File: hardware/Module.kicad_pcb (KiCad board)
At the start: 2 copper layers, 47.6 x 109.2 mm, 123 parts, among them J1 Jack, J10 Jack, J11 Jack, J12 Jack, J13 Micro_SD, J14 Jack, J15 Jack, J16 Jack, J17 Power, J18 Jack, J19 Jack, J2 OLED, J4 Jack, J5 Jack, J6 Jack, J7 Jack, J8 Jack, J9 Jack, SW1 Encoder, SW2 Encoder, U1 TL074, U2 TL074, U3 TL074, U4 MCP6004, U5 MCP6002, U6 TLP2361, U7 LM4040C10

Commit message: Release version 0.4.0
Signed-off-by: Petr Horacek <hrck@protonmail.com>
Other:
- board text added: "board v0.4.0"
- board text removed: "board v0.3.0"
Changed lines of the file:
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@@
     (title "Proton")
     (date "2022-03-06")
-    (rev "v0.3.0")
+    (rev "v0.4.0")
     (company "Petr Horáček")
     (comment 1 "petr@zlosynth.com")
@@
     (effects (font (size 1 1) (thickness 0.15)))
   )
-  (gr_text "board v0.3.0" (at 158.77 58.98 90) (layer "F.SilkS")
+  (gr_text "board v0.4.0" (at 158.77 58.98 90) (layer "F.SilkS")
     (effects (font (size 1 1) (thickness 0.15)) (justify left))
   )

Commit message: Release version 0.5.0
Signed-off-by: Petr Horacek <hrck@protonmail.com>
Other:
- board text added: "board v0.5.0"
- board text removed: "board v0.4.0"
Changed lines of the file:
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@@
     (title "Proton")
     (date "2022-03-06")
-    (rev "v0.4.0")
+    (rev "v0.5.0")
     (company "Petr Horáček")
     (comment 1 "petr@zlosynth.com")
@@
     (effects (font (size 1 1) (thickness 0.15)))
   )
-  (gr_text "board v0.4.0" (at 158.77 58.98 90) (layer "F.SilkS")
+  (gr_text "board v0.5.0" (at 158.77 58.98 90) (layer "F.SilkS")
     (effects (font (size 1 1) (thickness 0.15)) (justify left))
   )

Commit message: Place THT on two-layer PCB
Signed-off-by: Petr Horacek <hrck@protonmail.com>
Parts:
- removed C1: 100n, Capacitor_SMD:C_0603_1608Metric_Pad1.08x0.95mm_HandSolder
- removed D1: Schottky, Diode_SMD:D_SOD-123
- removed R21, R26, R27: 100k, Resistor_SMD:R_0603_1608Metric_Pad0.98x0.95mm_HandSolder
- removed R33: 100R, Resistor_SMD:R_0603_1608Metric_Pad0.98x0.95mm_HandSolder
- removed SW2: Encoder, Rotary_Encoder:RotaryEncoder_Alps_EC11E-Switch_Vertical_H20mm
- removed U6: TLP2361, Package_SO:SO-6L_10x3.84mm_P1.27mm
- added J20: Conn_02x08_Odd_Even, Connector_PinHeader_2.54mm:PinHeader_2x08_P2.54mm_Vertical, B.Cu at (144.6, 58.1)
- added J21: Conn_02x08_Odd_Even, Connector_PinSocket_2.54mm:PinSocket_2x08_P2.54mm_Vertical, F.Cu at (62.6, 56.9)
- added J22: Conn_02x08_Odd_Even, Connector_PinHeader_2.54mm:PinHeader_2x08_P2.54mm_Vertical, B.Cu at (119.5, 58.1)
- added J23: Conn_02x08_Odd_Even, Connector_PinHeader_2.54mm:PinHeader_2x08_P2.54mm_Vertical, B.Cu at (119.5, 93.0)
- added J3: Conn_02x08_Odd_Even, Connector_PinSocket_2.54mm:PinSocket_2x08_P2.54mm_Vertical, F.Cu at (37.5, 56.9)
- added REF**: MountingHole_3.2mm_M3, MountingHole:MountingHole_3.2mm_M3, F.Cu at (160.2, 117.5)
- added REF**: MountingHole_3.2mm_M3, MountingHole:MountingHole_3.2mm_M3, B.Cu at (78.2, 116.3)
- added RV1: Pot, Potentiometer_THT:Potentiometer_Alpha_RD901F-40-00D_Single_Vertical, B.Cu at (53.2, 87.2)
- J1, J4: footprint Custom:Jack_3.5mm_QingPu_WQP-PJ398SM_Vertical_CircularHoles_Stereo -> Connector_Audio:Jack_3.5mm_QingPu_WQP-PJ398SM_Vertical_CircularHoles
- J14: value Jack -> Conn_02x08_Odd_Even; footprint Connector_Audio:Jack_3.5mm_QingPu_WQP-PJ398SM_Vertical_CircularHoles -> Connector_PinSocket_2.54mm:PinSocket_2x08_P2.54mm_Vertical; moved to F.Cu
- R1: value 33R -> 33k
- R15, R20: value 100k -> 100R
- R2: value 220R -> 33k
- R3: value 10R -> 100k
- R9: value 33k -> 100k
- moved R20 255.5 mm to (-111.0, 121.3)
- moved R37 255.5 mm to (-125.2, 122.9)
- moved C11 255.5 mm to (-128.8, 130.7)
- moved C2 255.5 mm to (-121.2, 122.9)
- moved C3 255.5 mm to (-114.2, 133.5)
- moved C4 255.5 mm to (-130.5, 133.5)
- moved R1 255.5 mm to (-104.9, 127.7)
- moved R12 255.5 mm to (-121.2, 124.5)
- moved R13 255.5 mm to (-115.8, 133.5)
- moved R18 255.5 mm to (-120.7, 119.9)
- moved R30 255.5 mm to (-123.9, 120.0)
- moved R36 255.5 mm to (-132.2, 133.5)
- moved R5 255.5 mm to (-110.4, 125.4)
- moved U3 255.5 mm to (-123.2, 130.0)
- moved C10 255.5 mm to (-117.6, 130.6)
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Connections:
- net ENC1_A renamed ENC_A
- net ENC1_B renamed ENC_B
- net ENC1_CLICK renamed ENC_CLICK
- A1 pad 13: ENC2_CLICK -> unconnected-(A1-Pad13)
- A1 pad 14: ENC2_B -> unconnected-(A1-Pad14)
- A1 pad 15: ENC2_A -> unconnected-(A1-Pad15)
- A1 pad 32: MIDI_IN -> unconnected-(A1-Pad32)
- A1 pad 33: MIDI_OUT -> unconnected-(A1-Pad33)
- J1 pad T: Net-(D1-Pad2) -> Net-(J1-PadT)
- J11 pad TN: unconnected-(J11-PadTN) -> Net-(J11-PadTN)
- J12 pad TN: unconnected-(J12-PadTN) -> Net-(J12-PadTN)
- J16 pad TN: Net-(J16-PadTN) -> unconnected-(J16-PadTN)
- J19 pad TN: Net-(J19-PadTN) -> unconnected-(J19-PadTN)
- J2 pad 3: OLED_CS -> OLED_SCK
- J2 pad 4: OLED_CMD -> OLED_DATA
- J2 pad 6: OLED_DATA -> OLED_CMD
- J2 pad 7: OLED_SCK -> OLED_CS
- R1 pad 1: +3V3 -> GND
- R1 pad 2: Net-(J4-PadR) -> Net-(R1-Pad2)
- R15 pad 2: Net-(R15-Pad2) -> Net-(J8-PadT)
- R2 pad 1: Net-(J1-PadR) -> GND
- R2 pad 2: Net-(D1-Pad1) -> Net-(R2-Pad2)
- R20 pad 1: Net-(R14-Pad2) -> Net-(R20-Pad1)
- R20 pad 2: Net-(R20-Pad2) -> Net-(J7-PadT)
- R3 pad 1: MIDI_OUT -> Net-(R1-Pad2)
- R3 pad 2: Net-(J4-PadT) -> Net-(R15-Pad1)
- R32 pad 1: Net-(R26-Pad2) -> Net-(R14-Pad2)
- R32 pad 2: Net-(J7-PadT) -> Net-(J1-PadT)
- R4 pad 2: Net-(J5-PadTN) -> Net-(J15-PadTN)
- R40 pad 2: Net-(J11-PadT) -> Net-(J16-PadT)
- R41 pad 2: Net-(J12-PadT) -> Net-(J19-PadT)
- R45 pad 2: Net-(J16-PadTN) -> Net-(J12-PadTN)
- R46 pad 2: Net-(J15-PadTN) -> Net-(J6-PadTN)
- R47 pad 2: Net-(J14-PadTN) -> Net-(J4-PadTN)
- R49 pad 1: Net-(J18-PadT) -> Net-(J11-PadT)
- R5 pad 2: Net-(J6-PadTN) -> Net-(J18-PadTN)
- R51 pad 1: Net-(J19-PadT) -> Net-(J5-PadT)
- R53 pad 1: Net-(J14-PadT) -> Net-(J4-PadT)
- R57 pad 2: Net-(J18-PadTN) -> Net-(J11-PadTN)
- R58 pad 2: Net-(J19-PadTN) -> Net-(J5-PadTN)
- R6 pad 1: Net-(J5-PadT) -> Net-(J15-PadT)
- R60 pad 1: Net-(J15-PadT) -> Net-(J6-PadT)
- R62 pad 1: Net-(J16-PadT) -> Net-(J12-PadT)
- R7 pad 1: Net-(J6-PadT) -> Net-(J18-PadT)
- R8 pad 1: GATE1 -> GND
- R9 pad 1: GATE2 -> Net-(R2-Pad2)
- R9 pad 2: Net-(R15-Pad1) -> Net-(R20-Pad1)
- U1 pad 10: GND -> Net-(R1-Pad2)
- U1 pad 12: GND -> unconnected-(U1-Pad12)
- U1 pad 13: Net-(R21-Pad2) -> unconnected-(U1-Pad13)
- U1 pad 14: Net-(R27-Pad2) -> unconnected-(U1-Pad14)
- U1 pad 3: GND -> GATE1
- U1 pad 5: GND -> Net-(R2-Pad2)
- U1 pad 6: Net-(R20-Pad2) -> GATE2
- U1 pad 7: Net-(R26-Pad2) -> Net-(R20-Pad1)
- U1 pad 8: Net-(R15-Pad2) -> Net-(R15-Pad1)
- U1 pad 9: Net-(R15-Pad1) -> GATE3
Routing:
- net VCC: track 267.2 -> 0.00 mm, vias 7 -> 0
- net +3V3: track 178.6 -> 0.00 mm, vias 3 -> 0
- net VEE: track 156.2 -> 0.00 mm, vias 4 -> 0
- net GND: track 127.6 -> 0.00 mm, vias 37 -> 0
- net -10V: track 104.5 -> 0.00 mm, vias 13 -> 0
- net PROBE: track 102.1 -> 0.00 mm, vias 4 -> 0
- net MIDI_IN: track 94.9 -> 0.00 mm, vias 6 -> 0
- net +3.3VA: track 84.1 -> 0.00 mm, vias 9 -> 0
- net MIDI_OUT: track 81.4 -> 0.00 mm, vias 3 -> 0
- net DAC2: track 69.1 -> 0.00 mm, vias 4 -> 0
- net DAC1: track 64.7 -> 0.00 mm, vias 4 -> 0
- net GATE2: track 63.1 -> 0.00 mm, vias 2 -> 0
- net GATE1: track 59.2 -> 0.00 mm, vias 2 -> 0
- net CV3: track 53.5 -> 0.00 mm
- net CV2: track 49.2 -> 0.00 mm
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- removed copper zone on B.Cu, net GND
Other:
- board size 47.6 x 109.2 mm -> 129.5 x 110.4 mm
- board text added: "Jack"
- board text removed: "S. jack"
- board text removed: "Take care not to damage SMD parts while soldering"

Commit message: Wire up all connections
Signed-off-by: Petr Horacek <hrck@protonmail.com>
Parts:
- removed the REF** at (160.2, 117.5)
- removed the REF** at (78.2, 116.3)
- J14: value Conn_02x08_Odd_Even -> NW_B; footprint Connector_PinSocket_2.54mm:PinSocket_2x08_P2.54mm_Vertical -> Connector_PinSocket_2.54mm:PinSocket_2x06_P2.54mm_Vertical
- J20: value Conn_02x08_Odd_Even -> SW_B; footprint Connector_PinHeader_2.54mm:PinHeader_2x08_P2.54mm_Vertical -> Connector_PinSocket_2.54mm:PinSocket_2x06_P2.54mm_Vertical; moved to F.Cu
- J21: value Conn_02x08_Odd_Even -> NW_A; footprint Connector_PinSocket_2.54mm:PinSocket_2x08_P2.54mm_Vertical -> Connector_PinHeader_2.54mm:PinHeader_2x06_P2.54mm_Vertical; moved to B.Cu
- J22: value Conn_02x08_Odd_Even -> SW_A; footprint Connector_PinHeader_2.54mm:PinHeader_2x08_P2.54mm_Vertical -> Connector_PinHeader_2.54mm:PinHeader_2x06_P2.54mm_Vertical
- J23: value Conn_02x08_Odd_Even -> NE_A; footprint Connector_PinHeader_2.54mm:PinHeader_2x08_P2.54mm_Vertical -> Connector_PinHeader_2.54mm:PinHeader_2x06_P2.54mm_Vertical
- J3: value Conn_02x08_Odd_Even -> NE_B; footprint Connector_PinSocket_2.54mm:PinSocket_2x08_P2.54mm_Vertical -> Connector_PinSocket_2.54mm:PinSocket_2x06_P2.54mm_Vertical
- moved R1 262.5 mm to (152.0, 74.0), turned to 0 degrees
- moved R36 261.7 mm to (129.2, 122.0), turned to 180 degrees
- moved C11 260.3 mm to (131.5, 130.8), turned to -90 degrees
- moved C4 259.9 mm to (129.2, 124.4), turned to 0 degrees
- moved R31 257.2 mm to (130.6, 143.8), turned to 90 degrees
- moved R37 255.0 mm to (129.2, 140.2), turned to 0 degrees
- moved C5 254.8 mm to (129.2, 137.7), turned to 180 degrees
- moved R3 254.0 mm to (152.0, 76.2), turned to 0 degrees
- moved R30 253.4 mm to (128.4, 143.8), turned to 90 degrees
- moved U3 249.7 mm to (126.5, 131.4), turned to 0 degrees
- moved R19 248.1 mm to (124.7, 143.7), turned to -90 degrees
- moved C2 245.5 mm to (123.7, 140.2), turned to 0 degrees
- moved R12 245.3 mm to (123.8, 137.7), turned to 180 degrees
- moved R18 244.3 mm to (122.5, 143.8), turned to -90 degrees
- moved R13 240.2 mm to (124.2, 124.4), turned to 0 degrees
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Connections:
- A1 pad 10: OLED_CMD -> OLED_CMD_A
- A1 pad 11: OLED_DATA -> OLED_DATA_A
- A1 pad 2: SD_D3 -> SD_D3_A
- A1 pad 22: CV1 -> CV1_A
- A1 pad 23: CV5 -> CV5_A
- A1 pad 24: CV2 -> CV2_A
- A1 pad 25: CV3 -> CV3_A
- A1 pad 26: CV4 -> CV4_A
- A1 pad 27: ENC_CLICK -> POT_A
- A1 pad 28: ENC_A -> ENC_A_A
- A1 pad 3: SD_D2 -> SD_D2_A
- A1 pad 31: ENC_B -> ENC_B_A
- A1 pad 32: unconnected-(A1-Pad32) -> PROBE_A
- A1 pad 33: unconnected-(A1-Pad33) -> ENC_CLICK_A
- A1 pad 36: unconnected-(A1-Pad36) -> GATE3
- A1 pad 37: OLED_RST -> OLED_RST_A
- A1 pad 4: SD_D1 -> SD_D1_A
- A1 pad 5: SD_D0 -> SD_D0_A
- A1 pad 6: SD_CMD -> SD_CMD_A
- A1 pad 7: SD_CK -> SD_CK_A
- A1 pad 8: OLED_CS -> OLED_CS_A
- A1 pad 9: OLED_SCK -> OLED_SCK_A
- C12 pad 1: CV5 -> CV5_B
- C13 pad 1: CV3 -> CV3_B
- C14 pad 1: CV1 -> CV1_B
- C17 pad 1: CV2 -> CV2_B
- C18 pad 1: CV4 -> CV4_B
- C2 pad 2: Net-(C2-Pad2) -> AUDIO_IN2_JACK_A
- C3 pad 2: Net-(C3-Pad2) -> AUDIO_IN1_JACK_A
- C4 pad 1: Net-(C4-Pad1) -> AUDIO_OUT2_JACK_A
- C5 pad 1: Net-(C5-Pad1) -> AUDIO_OUT1_JACK_A
- D2 pad 3: PROBE -> PROBE_A
- J13 pad 1: SD_D2 -> SD_D2_B
- J13 pad 2: SD_D3 -> SD_D3_B
- J13 pad 3: SD_CMD -> SD_CMD_B
- J13 pad 5: SD_CK -> SD_CK_B
- J13 pad 7: SD_D0 -> SD_D0_B
- J13 pad 8: SD_D1 -> SD_D1_B
- J14 pad 1: unconnected-(J14-Pad1) -> SD_D1_B
- J14 pad 10: unconnected-(J14-Pad10) -> +3.3VA
- J14 pad 11: unconnected-(J14-Pad11) -> ENC_A_B
- J14 pad 12: unconnected-(J14-Pad12) -> ENC_B_B
- J14 pad 2: unconnected-(J14-Pad2) -> SD_D0_B
- J14 pad 3: unconnected-(J14-Pad3) -> SD_CK_B
- J14 pad 4: unconnected-(J14-Pad4) -> SD_CMD_B
- J14 pad 5: unconnected-(J14-Pad5) -> SD_D3_B
- J14 pad 6: unconnected-(J14-Pad6) -> SD_D2_B
- J14 pad 9: unconnected-(J14-Pad9) -> ENC_CLICK_B
- J2 pad 3: OLED_SCK -> OLED_SCK_B
- J2 pad 4: OLED_DATA -> OLED_DATA_B
- J2 pad 5: OLED_RST -> OLED_RST_B
- J2 pad 6: OLED_CMD -> OLED_CMD_B
- J2 pad 7: OLED_CS -> OLED_CS_B
- J20 pad 1: unconnected-(J20-Pad1) -> AUDIO_OUT1_JACK_B
- J20 pad 10: unconnected-(J20-Pad10) -> POT_B
- J20 pad 2: unconnected-(J20-Pad2) -> DAC2_JACK_B
- J20 pad 3: unconnected-(J20-Pad3) -> AUDIO_OUT2_JACK_B
- J20 pad 4: unconnected-(J20-Pad4) -> DAC1_JACK_B
- J20 pad 5: unconnected-(J20-Pad5) -> GATE3_JACK_B
- J20 pad 6: unconnected-(J20-Pad6) -> GATE2_JACK_B
- J20 pad 7: unconnected-(J20-Pad7) -> GATE1_JACK_B
- J20 pad 8: unconnected-(J20-Pad8) -> AUDIO_IN2_JACK_B
- J20 pad 9: unconnected-(J20-Pad9) -> AUDIO_IN1_JACK_B
- J21 pad 1: unconnected-(J21-Pad1) -> SD_D1_A
- J21 pad 10: unconnected-(J21-Pad10) -> +3.3VA
- J21 pad 11: unconnected-(J21-Pad11) -> ENC_A_A
- J21 pad 12: unconnected-(J21-Pad12) -> ENC_B_A
- J21 pad 2: unconnected-(J21-Pad2) -> SD_D0_A
- J21 pad 3: unconnected-(J21-Pad3) -> SD_CK_A
- J21 pad 4: unconnected-(J21-Pad4) -> SD_CMD_A
- J21 pad 5: unconnected-(J21-Pad5) -> SD_D3_A
- J21 pad 6: unconnected-(J21-Pad6) -> SD_D2_A
- J21 pad 9: unconnected-(J21-Pad9) -> ENC_CLICK_A
- J22 pad 1: unconnected-(J22-Pad1) -> AUDIO_OUT1_JACK_A
- J22 pad 10: unconnected-(J22-Pad10) -> POT_A
- J22 pad 2: unconnected-(J22-Pad2) -> DAC2_JACK_A
- J22 pad 3: unconnected-(J22-Pad3) -> AUDIO_OUT2_JACK_A
- J22 pad 4: unconnected-(J22-Pad4) -> DAC1_JACK_A
- J22 pad 5: unconnected-(J22-Pad5) -> GATE3_JACK_A
- J22 pad 6: unconnected-(J22-Pad6) -> GATE2_JACK_A
- J22 pad 7: unconnected-(J22-Pad7) -> GATE1_JACK_A
- J22 pad 8: unconnected-(J22-Pad8) -> AUDIO_IN2_JACK_A
- J22 pad 9: unconnected-(J22-Pad9) -> AUDIO_IN1_JACK_A
- J23 pad 1: unconnected-(J23-Pad1) -> +3V3
- J23 pad 10: unconnected-(J23-Pad10) -> CV1_A
- J23 pad 11: unconnected-(J23-Pad11) -> OLED_SCK_A
- J23 pad 12: unconnected-(J23-Pad12) -> PROBE_A
- J23 pad 2: unconnected-(J23-Pad2) -> CV5_A
- J23 pad 3: unconnected-(J23-Pad3) -> OLED_CS_A
- J23 pad 4: unconnected-(J23-Pad4) -> CV2_A
- J23 pad 5: unconnected-(J23-Pad5) -> OLED_CMD_A
- J23 pad 6: unconnected-(J23-Pad6) -> CV4_A
- J23 pad 7: unconnected-(J23-Pad7) -> OLED_RST_A
- J23 pad 8: unconnected-(J23-Pad8) -> CV3_A
- J23 pad 9: unconnected-(J23-Pad9) -> OLED_DATA_A
- J3 pad 1: unconnected-(J3-Pad1) -> +3V3
- J3 pad 10: unconnected-(J3-Pad10) -> CV1_B
- J3 pad 11: unconnected-(J3-Pad11) -> OLED_SCK_B
- J3 pad 12: unconnected-(J3-Pad12) -> PROBE_B
- J3 pad 2: unconnected-(J3-Pad2) -> CV5_B
- J3 pad 3: unconnected-(J3-Pad3) -> OLED_CS_B
- J3 pad 4: unconnected-(J3-Pad4) -> CV2_B
- J3 pad 5: unconnected-(J3-Pad5) -> OLED_CMD_B
- J3 pad 6: unconnected-(J3-Pad6) -> CV4_B
- J3 pad 7: unconnected-(J3-Pad7) -> OLED_RST_B
- J3 pad 8: unconnected-(J3-Pad8) -> CV3_B
- J3 pad 9: unconnected-(J3-Pad9) -> OLED_DATA_B
- R12 pad 1: Net-(C2-Pad2) -> AUDIO_IN2_JACK_A
- R13 pad 1: Net-(C3-Pad2) -> AUDIO_IN1_JACK_A
- R14 pad 2: Net-(R14-Pad2) -> GATE1_JACK_A
- R15 pad 1: Net-(R15-Pad1) -> GATE3_JACK_B
- R20 pad 1: Net-(R20-Pad1) -> GATE2_JACK_B
- R28 pad 2: Net-(R28-Pad2) -> DAC2_JACK_A
- R29 pad 2: Net-(R29-Pad2) -> DAC1_JACK_A
- R3 pad 2: Net-(R15-Pad1) -> GATE3_JACK_A
- R32 pad 1: Net-(R14-Pad2) -> GATE1_JACK_B
- R34 pad 1: Net-(R28-Pad2) -> DAC2_JACK_B
- R35 pad 1: Net-(R29-Pad2) -> DAC1_JACK_B
- R36 pad 2: Net-(C4-Pad1) -> AUDIO_OUT2_JACK_A
- R37 pad 2: Net-(C5-Pad1) -> AUDIO_OUT1_JACK_A
- R38 pad 2: SD_D1 -> SD_D1_B
- R39 pad 2: SD_D0 -> SD_D0_B
- R4 pad 1: PROBE -> PROBE_B
- R40 pad 1: Net-(C4-Pad1) -> AUDIO_OUT2_JACK_B
- R41 pad 1: Net-(C5-Pad1) -> AUDIO_OUT1_JACK_B
- R42 pad 2: SD_CMD -> SD_CMD_B
- R43 pad 2: SD_D3 -> SD_D3_B
- R44 pad 2: SD_D2 -> SD_D2_B
- R45 pad 1: PROBE -> PROBE_B
- R46 pad 1: PROBE -> PROBE_B
- R47 pad 1: PROBE -> PROBE_B
- R5 pad 1: PROBE -> PROBE_B
- R54 pad 2: CV5 -> CV5_B
- R55 pad 2: CV3 -> CV3_B
- R56 pad 2: CV1 -> CV1_B
- R57 pad 1: PROBE -> PROBE_B
- R58 pad 1: PROBE -> PROBE_B
- R6 pad 2: Net-(C2-Pad2) -> AUDIO_IN2_JACK_B
- R64 pad 2: CV2 -> CV2_B
- R65 pad 2: CV4 -> CV4_B
- R7 pad 2: Net-(C3-Pad2) -> AUDIO_IN1_JACK_B
- R9 pad 2: Net-(R20-Pad1) -> GATE2_JACK_A
- RV1 pad 2: POT -> POT_B
- SW1 pad A: ENC_A -> ENC_A_B
- SW1 pad B: ENC_B -> ENC_B_B
- SW1 pad S1: ENC_CLICK -> ENC_CLICK_B
- U1 pad 1: Net-(R14-Pad2) -> GATE1_JACK_A
- U1 pad 7: Net-(R20-Pad1) -> GATE2_JACK_A
- U1 pad 8: Net-(R15-Pad1) -> GATE3_JACK_A
- U2 pad 14: Net-(R28-Pad2) -> DAC2_JACK_A
- U2 pad 7: Net-(R29-Pad2) -> DAC1_JACK_A
- U3 pad 14: Net-(C4-Pad1) -> AUDIO_OUT2_JACK_A
- U3 pad 2: Net-(C3-Pad2) -> AUDIO_IN1_JACK_A
- U3 pad 6: Net-(C2-Pad2) -> AUDIO_IN2_JACK_A
- U3 pad 8: Net-(C5-Pad1) -> AUDIO_OUT1_JACK_A
- U4 pad 1: CV2 -> CV2_B
- U4 pad 14: CV3 -> CV3_B
- U4 pad 7: CV5 -> CV5_B
- U4 pad 8: CV4 -> CV4_B
- U5 pad 1: CV1 -> CV1_B
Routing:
- net VCC: track 0.00 -> 185.8 mm, vias 0 -> 16
- net +3.3VA: track 0.00 -> 185.4 mm, vias 0 -> 15
- net PROBE_B: track 0.00 -> 183.7 mm, vias 0 -> 3
- net Net-(R49-Pad2): track 0.00 -> 136.8 mm
- net +3V3: track 0.00 -> 123.7 mm, vias 0 -> 6
- net VEE: track 0.00 -> 119.9 mm, vias 0 -> 11
- net Net-(C18-Pad2): track 0.00 -> 110.7 mm
- net Net-(C17-Pad2): track 0.00 -> 109.7 mm, vias 0 -> 2
- net CV5_A: track 0.00 -> 104.3 mm, vias 0 -> 2
- net OLED_DATA_A: track 0.00 -> 103.4 mm, vias 0 -> 1
- net CV1_A: track 0.00 -> 103.2 mm, vias 0 -> 2
- net CV2_A: track 0.00 -> 101.4 mm, vias 0 -> 2
- net ENC_A_A: track 0.00 -> 101.1 mm, vias 0 -> 2
- net Net-(C13-Pad2): track 0.00 -> 99.5 mm
- net OLED_CMD_A: track 0.00 -> 98.3 mm, vias 0 -> 1
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- added copper zone on B.Cu, net GND
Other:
- board text added: "RED-12V"
- board text removed: "-"
- board text removed: "RED -12 V"

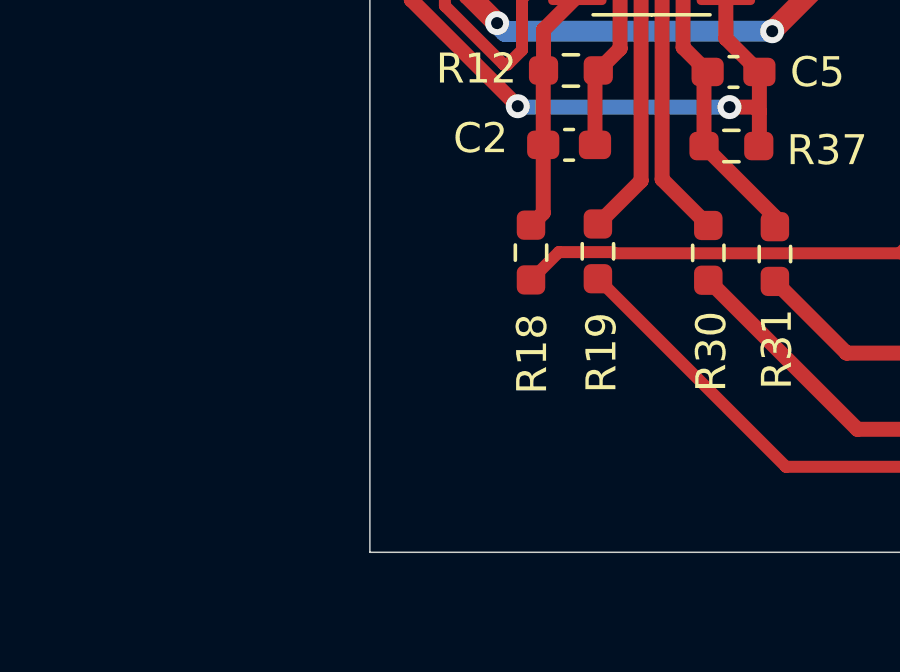
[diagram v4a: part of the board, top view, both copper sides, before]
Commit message: Add extension socket
It could be hotwired to unused pins of daisy using wires.

Signed-off-by: Petr Horacek <hrck@protonmail.com>
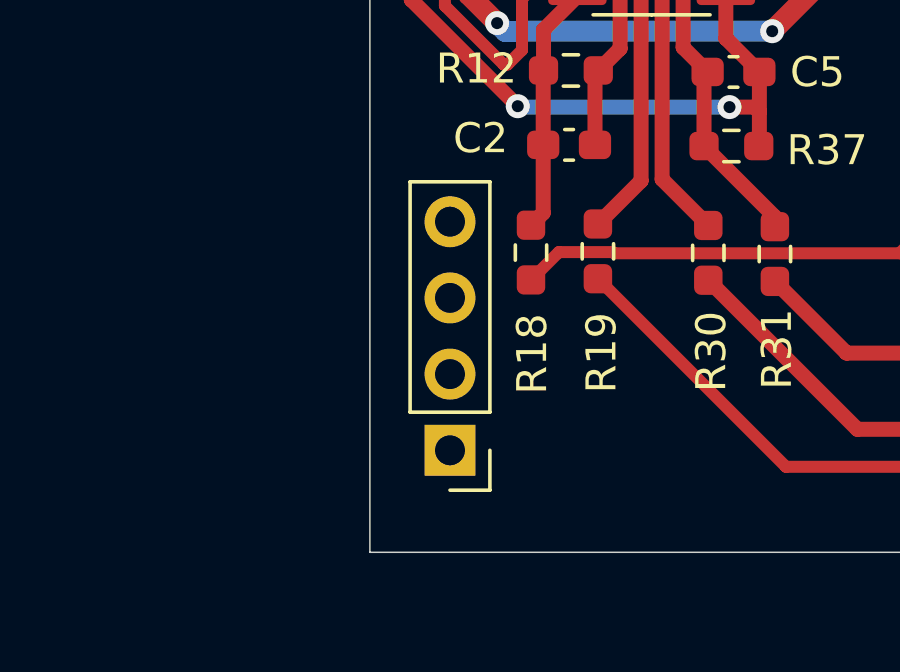
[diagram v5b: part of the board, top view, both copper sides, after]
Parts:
- added locked: EXT, Connector_PinHeader_2.54mm:PinHeader_1x04_P2.54mm_Vertical, F.Cu at (119.8, 150.3)
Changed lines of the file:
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@@
+    )
+  )
+  (footprint "Connector_PinHeader_2.54mm:PinHeader_1x04_P2.54mm_Vertical" (layer "F.Cu")
+    (at 119.77 150.35 180)
+    (descr "Through hole straight pin header, 1x04, 2.54mm pitch, single row")
+    (tags "Through hole pin header THT 1x04 2.54mm single row")
+    (attr through_hole)
+    (fp_text reference locked "REF**" (at 0 -2.33) (layer "F.SilkS") hide
+      (effects (font (size 1 1) (thickness 0.15)))
+    )
+    (fp_text value "EXT" (at 0 9.95) (layer "F.Fab") hide
+      (effects (font (size 1 1) (thickness 0.15)))
+    )
+    (fp_text user "${REFERENCE}" (at 0 3.81 90) (layer "F.Fab")
+      (effects (font (size 1 1) (thickness 0.15)))
+    )
+    (fp_line (start -1.33 0) (end -1.33 -1.33) (layer "F.SilkS") (width 0.12))
+    (fp_line (start 1.33 1.27) (end 1.33 8.95) (layer "F.SilkS") (width 0.12))
+    (fp_line (start -1.33 1.27) (end 1.33 1.27) (layer "F.SilkS") (width 0.12))
+    (fp_line (start -1.33 -1.33) (end 0 -1.33) (layer "F.SilkS") (width 0.12))
+    (fp_line (start -1.33 1.27) (end -1.33 8.95) (layer "F.SilkS") (width 0.12))
+    (fp_line (start -1.33 8.95) (end 1.33 8.95) (layer "F.SilkS") (width 0.12))
+    (fp_line (start 1.8 -1.8) (end -1.8 -1.8) (layer "F.CrtYd") (width 0.05))
+    (fp_line (start -1.8 -1.8) (end -1.8 9.4) (layer "F.CrtYd") (width 0.05))
+    (fp_line (start 1.8 9.4) (end 1.8 -1.8) (layer "F.CrtYd") (width 0.05))
+    (fp_line (start -1.8 9.4) (end 1.8 9.4) (layer "F.CrtYd") (width 0.05))
+    (fp_line (start -1.27 8.89) (end -1.27 -0.635) (layer "F.Fab") (width 0.1))
+    (fp_line (start -1.27 -0.635) (end -0.635 -1.27) (layer "F.Fab") (width 0.1))
+    (fp_line (start 1.27 8.89) (end -1.27 8.89) (layer "F.Fab") (width 0.1))
+    (fp_line (start 1.27 -1.27) (end 1.27 8.89) (layer "F.Fab") (width 0.1))
+    (fp_line (start -0.635 -1.27) (end 1.27 -1.27) (layer "F.Fab") (width 0.1))
+    (pad "1" thru_hole rect (at 0 0 180) (size 1.7 1.7) (drill 1) (layers *.Cu *.Mask))
+    (pad "2" thru_hole oval (at 0 2.54 180) (size 1.7 1.7) (drill 1) (layers *.Cu *.Mask))
+    (pad "3" thru_hole oval (at 0 5.08 180) (size 1.7 1.7) (drill 1) (layers *.Cu *.Mask))
+    (pad "4" thru_hole oval (at 0 7.62 180) (size 1.7 1.7) (drill 1) (layers *.Cu *.Mask))
+    (model "${KICAD6_3DMODEL_DIR}/Connector_PinHeader_2.54mm.3dshapes/PinHeader_1x04_P2.54mm_Vertical.wrl"
+      (offset (xyz 0 0 0))
+      (scale (xyz 1 1 1))
+      (rotate (xyz 0 0 0))
     )
   )
